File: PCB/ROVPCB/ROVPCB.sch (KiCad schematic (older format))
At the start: 24 parts, among them J1 Conn_01x04_Male, J2 Conn_01x04_Male, J3 Conn_01x02_Male, J4 Conn_01x01_Male, P1 Conn_02x20_Odd_Even, U1 MPU-9250, U2 BME280, U3 LIGHT_TSL2591, U4 LTC4316IDDPBF, U5 AtlasOEM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

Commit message: Adding mas Documentation
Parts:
- U3: symbol Adafruit_TSL2591-eagle-import:LIGHT_TSL2591 -> ROVPCB-rescue:LIGHT_TSL2591-Adafruit_TSL2591-eagle-import
- U4: symbol LTC4316IDDPBF:LTC4316IDDPBF -> ROVPCB-rescue:LTC4316IDDPBF-LTC4316IDDPBF
- U5: symbol Adafruit_TSL2591-eagle-import:AtlasOEM -> ROVPCB-rescue:AtlasOEM-Adafruit_TSL2591-eagle-import
- U6: symbol Adafruit_TSL2591-eagle-import:LTC2451CTS8-TRMPBF -> ROVPCB-rescue:LTC2451CTS8-TRMPBF-Adafruit_TSL2591-eagle-import
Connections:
- net GND: no longer U4.11 (GND)
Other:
- note added: "Press"
- note added: "Temp"
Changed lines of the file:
@@
 F 1 "Conn_01x04_Male" H 4856 1687 50  0000 C CNN
 F 2 "Connector_Hirose:Hirose_DF13-04P-1.25DSA_1x04_P1.25mm_Vertical" H 4750 1500 50  0001 C CNN
-F 3 "~" H 4750 1500 50  0001 C CNN
+F 3 "${KIPRJMOD}\\Datasheets\\BlueRobotics_TSYS01.pdf" H 4750 1500 50  0001 C CNN
 F 4 "DF13-04P-1.25DSA" H 4750 1500 50  0001 C CNN "manf#"
 	1    4750 1500
@@
 F 1 "Conn_01x04_Male" H 4856 2187 50  0000 C CNN
 F 2 "Connector_Hirose:Hirose_DF13-04P-1.25DSA_1x04_P1.25mm_Vertical" H 4750 2000 50  0001 C CNN
-F 3 "~" H 4750 2000 50  0001 C CNN
+F 3 "${KIPRJMOD}\\Datasheets\\BlueRobotics_MS5837.pdf" H 4750 2000 50  0001 C CNN
 F 4 "DF13-04P-1.25DSA" H 4750 2000 50  0001 C CNN "manf#"
 	1    4750 2000
@@
 Lux
 $Comp
-L Adafruit_TSL2591-eagle-import:LIGHT_TSL2591 U3
+L ROVPCB-rescue:LIGHT_TSL2591-Adafruit_TSL2591-eagle-import U3
 U 1 1 5CB6F38A
 P 5150 7050
@@
 I2C Address Translator
 $Comp
-L LTC4316IDDPBF:LTC4316IDDPBF U4
+L ROVPCB-rescue:LTC4316IDDPBF-LTC4316IDDPBF U4
 U 1 1 5CBEE417
 P 9900 5650
@@
 $EndComp
 $Comp
-L Adafruit_TSL2591-eagle-import:AtlasOEM U5
+L ROVPCB-rescue:AtlasOEM-Adafruit_TSL2591-eagle-import U5
 U 1 1 5CBE687D
 P 8650 1400
@@
 	6800 5350 6300 5350
 $Comp
-L Adafruit_TSL2591-eagle-import:LTC2451CTS8-TRMPBF U6
+L ROVPCB-rescue:LTC2451CTS8-TRMPBF-Adafruit_TSL2591-eagle-import U6
 U 1 1 5CC0994E
 P 7600 2850
@@
 Text Notes 8325 2425 0    50   ~ 0
 Default I2C address: 0x14
+Text Notes 4375 1575 0    79   ~ 16
+Temp
+Text Notes 4375 2075 0    79   ~ 16
+Press
 $EndSCHEMATC

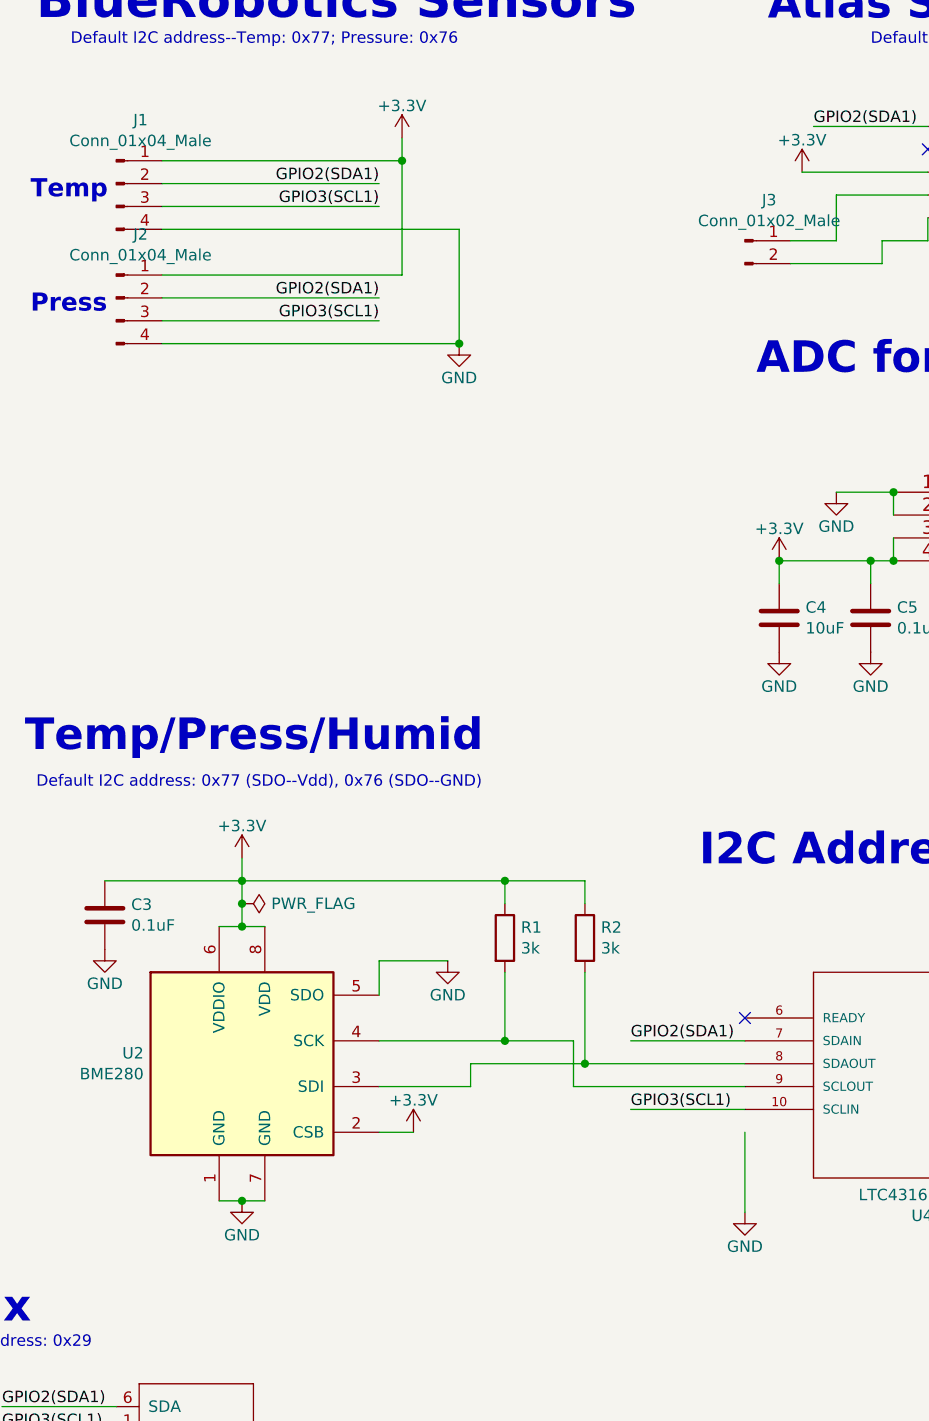
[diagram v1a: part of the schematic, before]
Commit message: Stupid i2c inputs were flipped.....
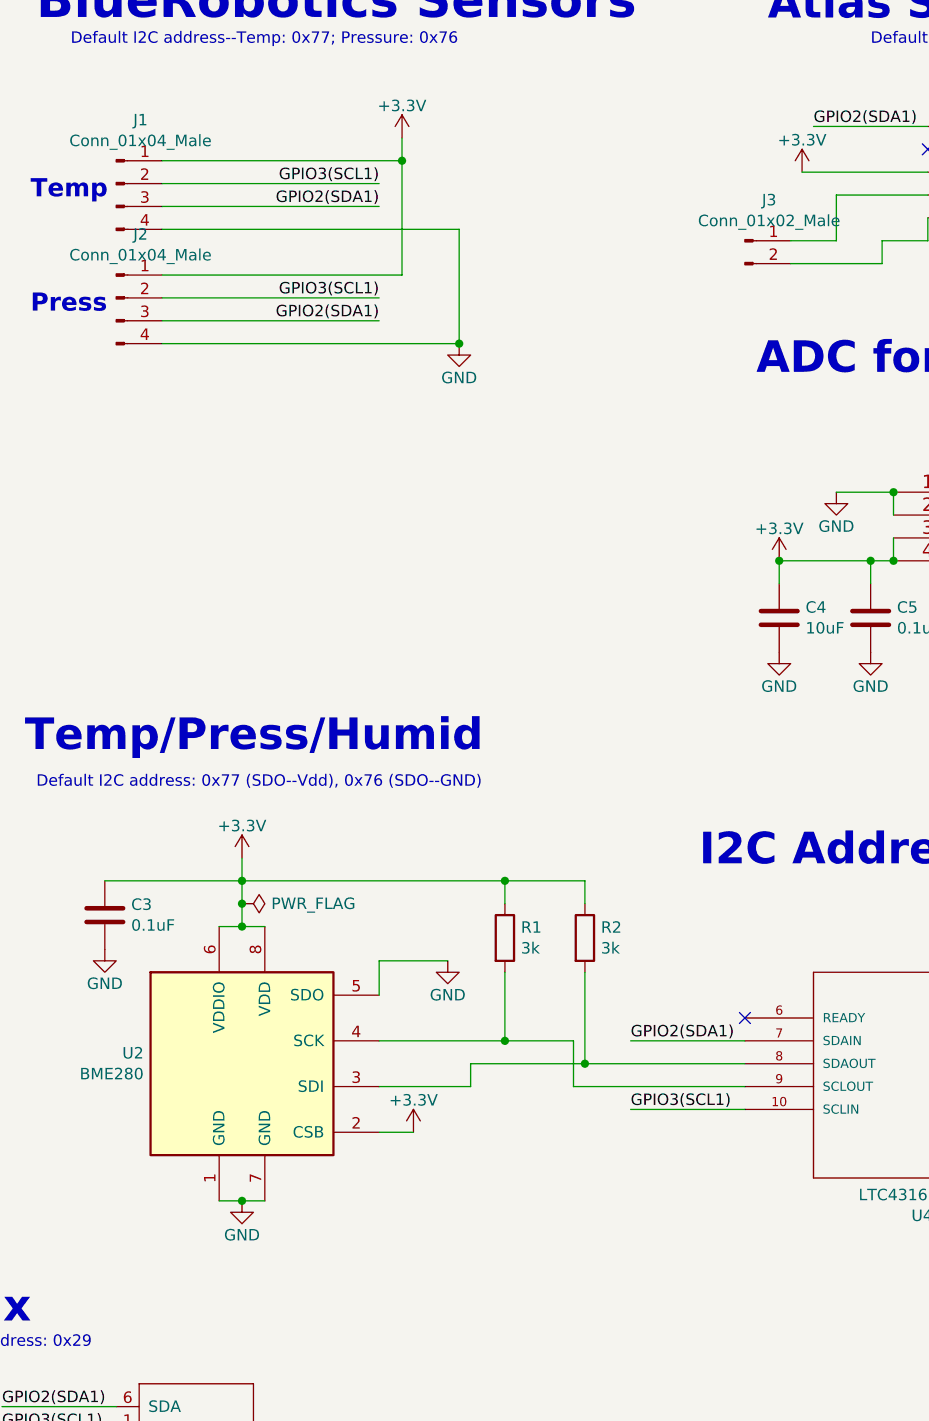
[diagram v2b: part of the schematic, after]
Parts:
- U1: footprint Sensor_Motion:InvenSense_QFN-24_3x3mm_P0.4mm -> Sensor_Motion:InvenSense_QFN-24_4x4mm_P0.5mm
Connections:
- net GPIO2(SDA1): now also J1.3 (Pin_3), J2.3 (Pin_3); no longer J1.2 (Pin_2), J2.2 (Pin_2)
- net GPIO3(SCL1): now also J1.2 (Pin_2), J2.2 (Pin_2); no longer J1.3 (Pin_3), J2.3 (Pin_3)
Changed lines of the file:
@@
 Text Notes 4400 800  0    157  ~ 31
 BlueRobotics Sensors
+Text Label 5900 1600 2    50   ~ 0
+GPIO2(SDA1)
 Text Label 5900 1500 2    50   ~ 0
-GPIO2(SDA1)
-Text Label 5900 1600 2    50   ~ 0
 GPIO3(SCL1)
 $Comp
@@
 	6000 1900 6000 1400
 Connection ~ 6000 1400
+Text Label 5900 2100 2    50   ~ 0
+GPIO2(SDA1)
 Text Label 5900 2000 2    50   ~ 0
-GPIO2(SDA1)
-Text Label 5900 2100 2    50   ~ 0
 GPIO3(SCL1)
 Wire Wire Line
-	5900 1500 4950 1500
-Wire Wire Line
-	4950 1600 5900 1600
-Wire Wire Line
-	5900 2000 4950 2000
-Wire Wire Line
-	4950 2100 5900 2100
+	5900 1600 4950 1600
+Wire Wire Line
+	4950 1500 5900 1500
+Wire Wire Line
+	5900 2100 4950 2100
+Wire Wire Line
+	4950 2000 5900 2000
 Text Notes 1600 3750 0    157  ~ 31
 Accelerometer
@@
 F 0 "U1" H 2450 4314 50  0000 C CNN
 F 1 "MPU-9250" H 2450 4223 50  0000 C CNN
-F 2 "Sensor_Motion:InvenSense_QFN-24_3x3mm_P0.4mm" H 2450 4300 50  0001 C CNN
+F 2 "Sensor_Motion:InvenSense_QFN-24_4x4mm_P0.5mm" H 2450 4300 50  0001 C CNN
 F 3 "${KIPRJMOD}\\Datasheets\\MPU9250.pdf" H 2450 5150 50  0001 C CNN
 F 4 "MPU-9250" H 2450 5300 50  0001 C CNN "manf#"
@@
 Text Notes 7300 4500 0    138  ~ 28
 I2C Address Translator
-$Comp
-L ROVPCB-rescue:LTC4316IDDPBF-LTC4316IDDPBF U4
-U 1 1 5CBEE417
-P 9900 5650
-F 0 "U4" H 11525 6015 50  0000 C CNN
-F 1 "LTC4316IDDPBF" H 11525 5924 50  0000 C CNN
-F 2 "Package_SO:MSOP-10_3x3mm_P0.5mm" H 13450 5150 50  0001 L BNN
-F 3 "${KIPRJMOD}\\Datasheets\\LTC4316.pdf" H 13250 5650 50  0001 L BNN
-F 4 "Linear Technology/Analog" H 13100 5950 50  0001 L BNN "Field4"
-F 5 "LTC4316 - Single I2C/SMBus Address Translator" H 12700 5800 50  0001 L BNN "Field5"
-F 6 "LTC4316IDD#PBF" H 13350 5300 50  0001 L BNN "Field7"
-F 7 "DFN-10 Linear Technology" H 13150 5500 50  0001 L BNN "Field8"
-F 8 "LTC4316IDD" H 9900 5650 50  0001 C CNN "manf#"
-	1    9900 5650
-	-1   0    0    1
-$EndComp
 Text Notes 7600 800  0    138  ~ 28
 Atlas Scientific board
@@
 Wire Wire Line
 	7000 5250 7500 5250
-$Comp
-L ROVPCB-rescue:GND-power-ROVPCB-rescue-ROVPCB-rescue-ROVPCB-rescue #PWR0111
-U 1 1 5CB8FA80
-P 7500 6000
-F 0 "#PWR0111" H 7500 5750 50  0001 C CNN
-F 1 "GND" H 7500 5850 50  0000 C CNN
-F 2 "" H 7500 6000 50  0000 C CNN
-F 3 "" H 7500 6000 50  0000 C CNN
-	1    7500 6000
-	1    0    0    -1
-$EndComp
-Wire Wire Line
-	7500 5650 7500 6000
 Wire Wire Line
 	7500 5350 6800 5350
@@
 Text Notes 4375 2075 0    79   ~ 16
 Press
+$Comp
+L ROVPCB-rescue:LTC4316IDDPBF-LTC4316IDDPBF U4
+U 1 1 5CBEE417
+P 9900 5650
+F 0 "U4" H 11525 6015 50  0000 C CNN
+F 1 "LTC4316IDDPBF" H 11525 5924 50  0000 C CNN
+F 2 "Package_SO:MSOP-10_3x3mm_P0.5mm" H 13450 5150 50  0001 L BNN
+F 3 "${KIPRJMOD}\\Datasheets\\LTC4316.pdf" H 13250 5650 50  0001 L BNN
+F 4 "Linear Technology/Analog" H 13100 5950 50  0001 L BNN "Field4"
+F 5 "LTC4316 - Single I2C/SMBus Address Translator" H 12700 5800 50  0001 L BNN "Field5"
+F 6 "LTC4316IDD#PBF" H 13350 5300 50  0001 L BNN "Field7"
+F 7 "DFN-10 Linear Technology" H 13150 5500 50  0001 L BNN "Field8"
+F 8 "LTC4316IDD" H 9900 5650 50  0001 C CNN "manf#"
+	1    9900 5650
+	-1   0    0    1
+$EndComp
 $EndSCHEMATC

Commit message: The correct footprint.... DUMB
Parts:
- U1: footprint Sensor_Motion:InvenSense_QFN-24_4x4mm_P0.5mm -> Sensor_Motion:InvenSense_QFN-24_3x3mm_P0.4mm
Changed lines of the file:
@@
 F 0 "U1" H 2450 4314 50  0000 C CNN
 F 1 "MPU-9250" H 2450 4223 50  0000 C CNN
-F 2 "Sensor_Motion:InvenSense_QFN-24_4x4mm_P0.5mm" H 2450 4300 50  0001 C CNN
+F 2 "Sensor_Motion:InvenSense_QFN-24_3x3mm_P0.4mm" H 2450 4300 50  0001 C CNN
 F 3 "${KIPRJMOD}\\Datasheets\\MPU9250.pdf" H 2450 5150 50  0001 C CNN
 F 4 "MPU-9250" H 2450 5300 50  0001 C CNN "manf#"
